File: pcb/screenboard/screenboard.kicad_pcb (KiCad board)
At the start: 2 copper layers, 223.5 x 176 mm, 72 parts, among them J1 0.5mm, J2 I-PEX, J3 1mm, J4 0.5mm, J5 0.5mm, U1 DS90CR286, U2 TPS65185

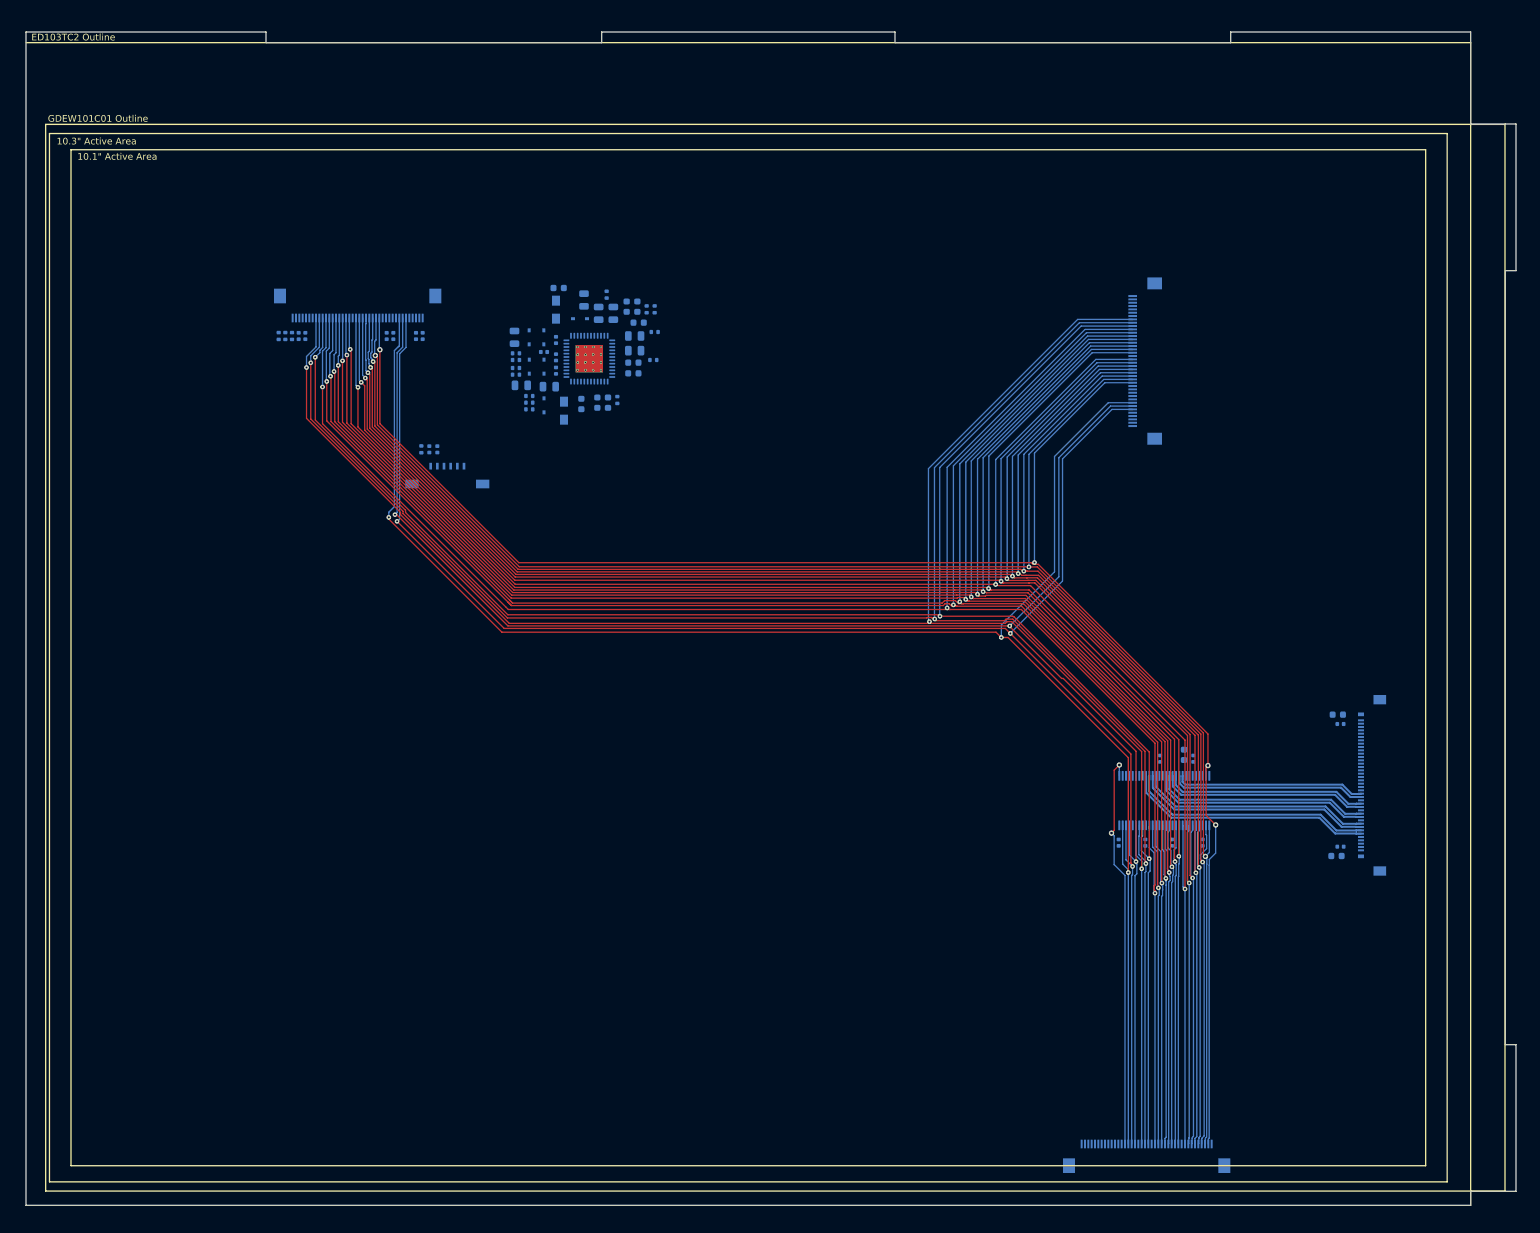
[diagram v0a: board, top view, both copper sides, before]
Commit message: - pcb: migrate to latest kicad, r0p1
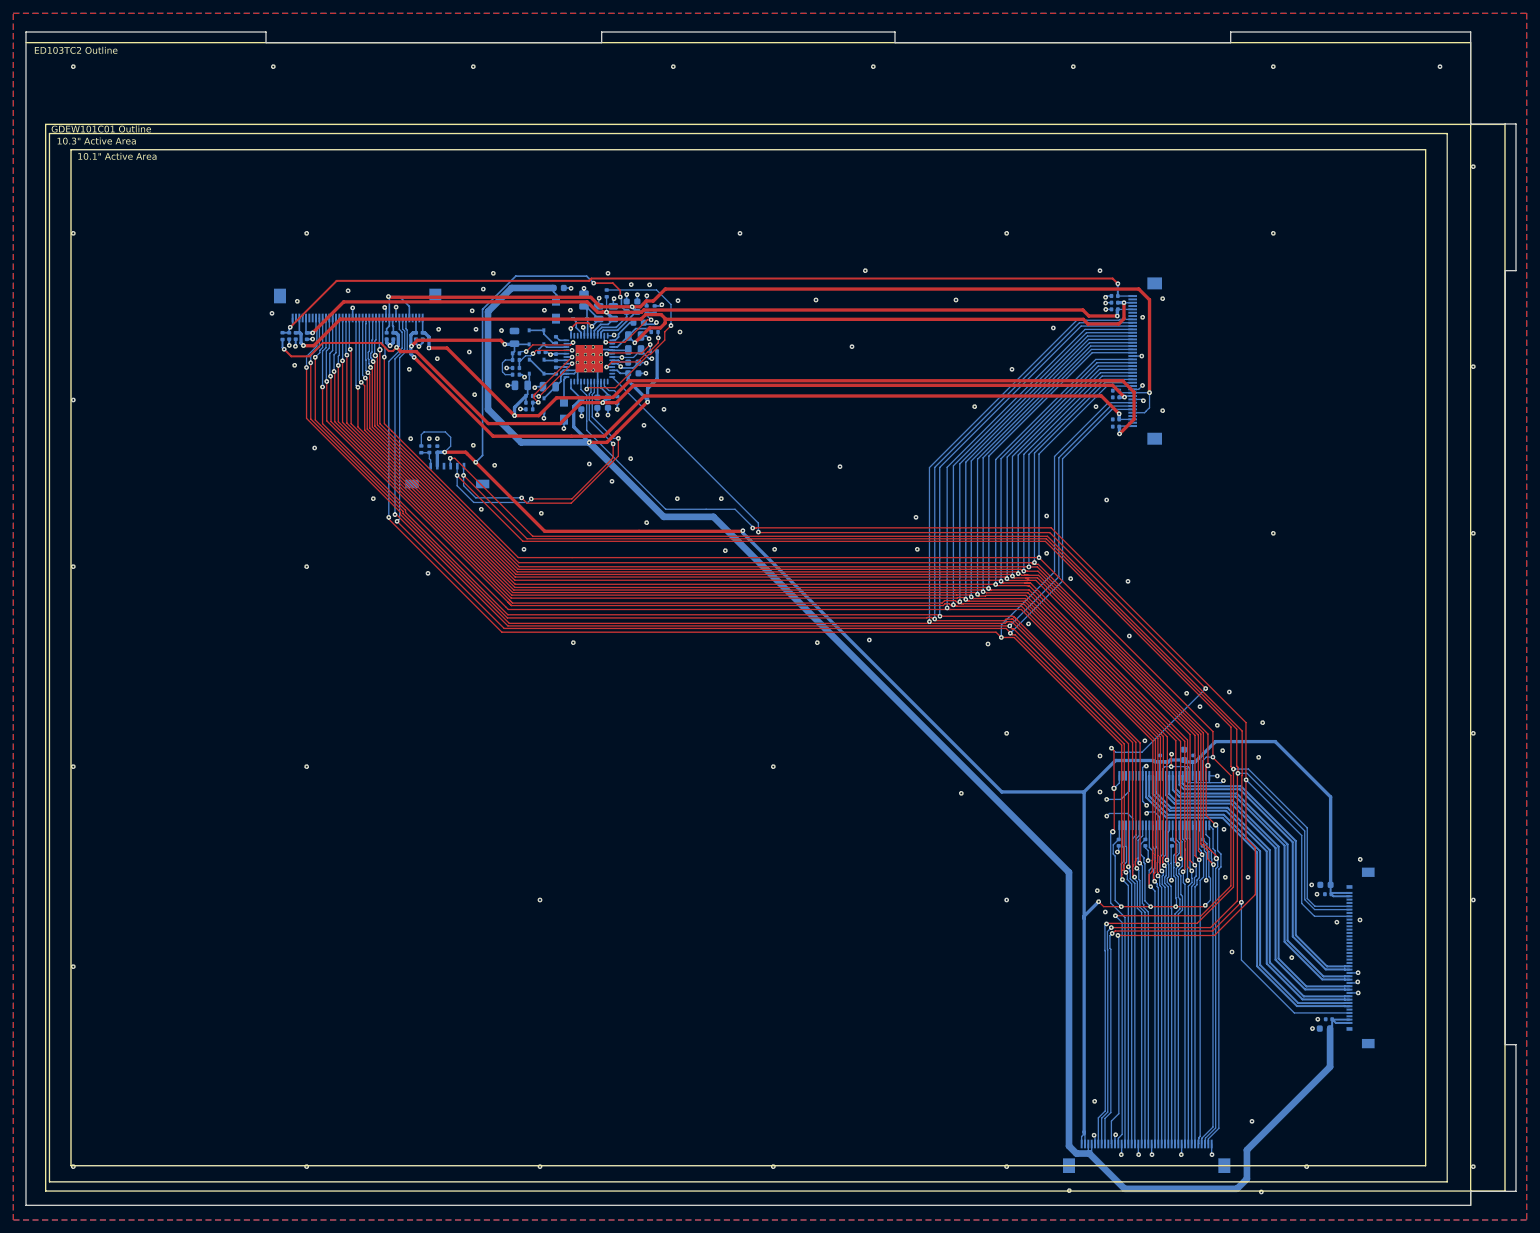
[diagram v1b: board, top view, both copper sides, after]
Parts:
- removed R14, R15: NC, Resistor_SMD:R_0402_1005Metric
- added C41: 220nF, Capacitor_SMD:C_0402_1005Metric, B.Cu at (266.2, 99.4)
- added C42: 220nF, Capacitor_SMD:C_0402_1005Metric, B.Cu at (266.4, 119.0)
- added C43: 220nF, Capacitor_SMD:C_0402_1005Metric, B.Cu at (266.4, 117.9)
- added C44: 220nF, Capacitor_SMD:C_0402_1005Metric, B.Cu at (266.4, 113.6)
- added C45: 220nF, Capacitor_SMD:C_0402_1005Metric, B.Cu at (266.4, 114.6)
- added C46: 220nF, Capacitor_SMD:C_0402_1005Metric, B.Cu at (266.2, 101.4)
- added C47: 220nF, Capacitor_SMD:C_0402_1005Metric, B.Cu at (266.2, 100.4)
- added C48: 220nF, Capacitor_SMD:C_0402_1005Metric, B.Cu at (142.4, 105.4)
- moved C1 25.9 mm to (298.3, 207.9)
- moved C3 25.9 mm to (297.7, 209.3)
- moved J2 25.9 mm to (301.9, 198.7)
- moved C8 25.6 mm to (297.8, 187.7)
- moved C6 25.6 mm to (298.2, 189.1)
- moved R16 1.42 mm to (141.4, 105.4)
- moved R9 1.31 mm to (197.1, 107.7)
- moved C33 0.44 mm to (143.4, 105.4)
- moved C12 0.27 mm to (180.3, 107.8)
- moved C34 0.23 mm to (145.0, 105.4)
- moved R7 0.19 mm to (190.0, 99.0)
- moved C23 0.11 mm to (194.2, 107.5)
- moved C10 0.10 mm to (191.0, 101.9)
- moved C16 0.10 mm to (188.8, 101.9)
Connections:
- J1 pad 32: /EPD_PWROK -> (no net)
- J2 pad 37: (no net) -> /EPD_TP_INT
- J5 pad 2: unconnected-(J5-Pad2) -> (no net)
- J5 pad 34: unconnected-(J5-Pad34) -> (no net)
- J5 pad 35: unconnected-(J5-Pad35) -> (no net)
- J5 pad 37: unconnected-(J5-Pad37) -> (no net)
- J5 pad 39: unconnected-(J5-Pad39) -> (no net)
- J5 pad 4: unconnected-(J5-Pad4) -> (no net)
- U2 pad 23: /EPD_PWROK -> (no net)
- U2 pad 49: GND -> Net-(C23-Pad1)
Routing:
- net +3V3: track 0.00 -> 382.4 mm, vias 0 -> 10
- net +5V: track 0.00 -> 291.5 mm, vias 0 -> 2
- net /I2C_SDA: track 0.00 -> 286.1 mm, vias 0 -> 5
- net /I2C_SCL: track 0.00 -> 286.0 mm, vias 0 -> 5
- net /EPDC_SDCLK: track 0.00 -> 275.6 mm, vias 0 -> 4
- net /EPD_TP_INT: track 0.00 -> 244.3 mm, vias 0 -> 3
- net /EPD_PWR_EN: track 0.00 -> 236.2 mm, vias 0 -> 3
- net +3V3_LCD: track 0.00 -> 159.8 mm, vias 0 -> 3
- net VNEG: track 0.00 -> 150.6 mm, vias 0 -> 3
- net VGH: track 0.00 -> 149.5 mm, vias 0 -> 4
- net VCOM: track 0.00 -> 148.6 mm, vias 0 -> 4
- net GND: track 0.00 -> 143.7 mm, vias 0 -> 201
- net VPOS: track 0.00 -> 138.9 mm, vias 0 -> 3
- net VGL: track 0.00 -> 136.5 mm, vias 0 -> 3
- net /BORDER: track 0.00 -> 135.0 mm, vias 0 -> 2
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- added copper zone on B.Cu, net GND
- added copper zone on F.Cu, net GND
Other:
- board text added: "Archer"
- board text added: "Copyright 2021 EI2030"
- board text added: "Screen Board r0.1"
